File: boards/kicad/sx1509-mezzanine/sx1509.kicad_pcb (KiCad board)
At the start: 2 copper layers, 85 x 34.3 mm, 19 parts, among them J1 Conn_02x08_Odd_Even, J2 Conn_02x08_Odd_Even, J3 Conn_01x02_Male, J4 Conn_01x02_Male, P1 CONN_02X20, P2 CONN_02X20, U1 SX1509

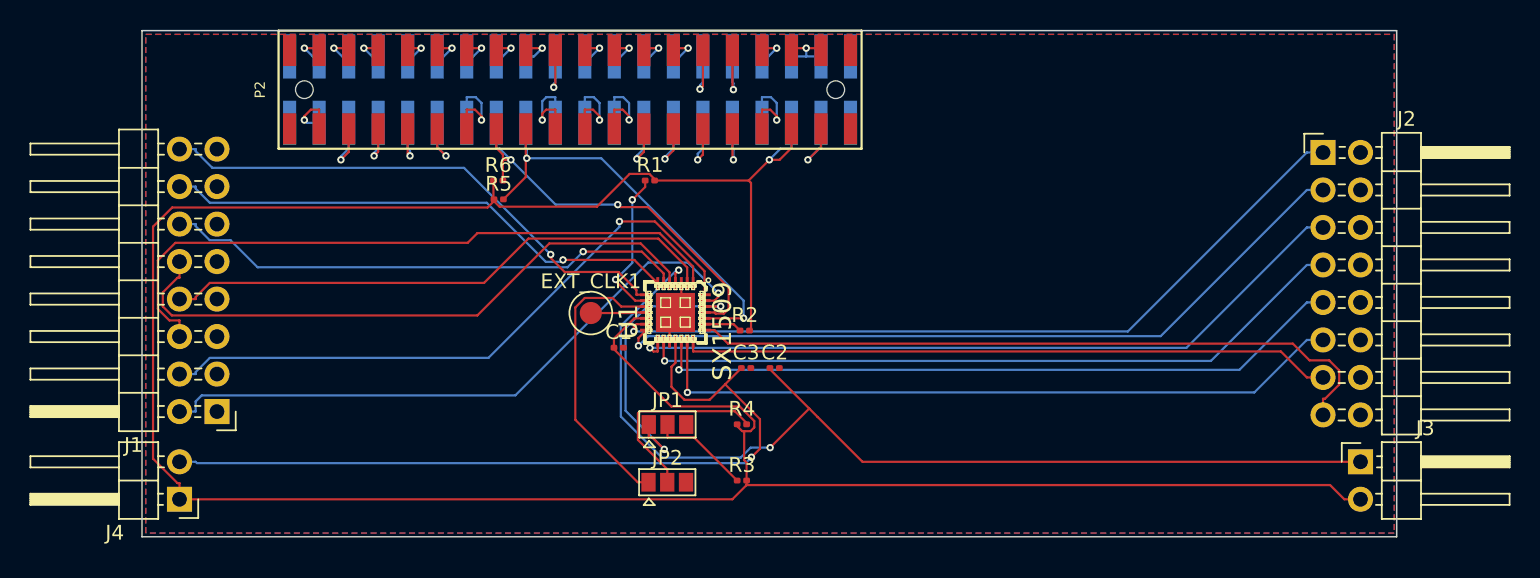
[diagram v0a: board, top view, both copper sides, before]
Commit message: Clean up design
The placement, routing, and silkscreen were updated to look nicer.
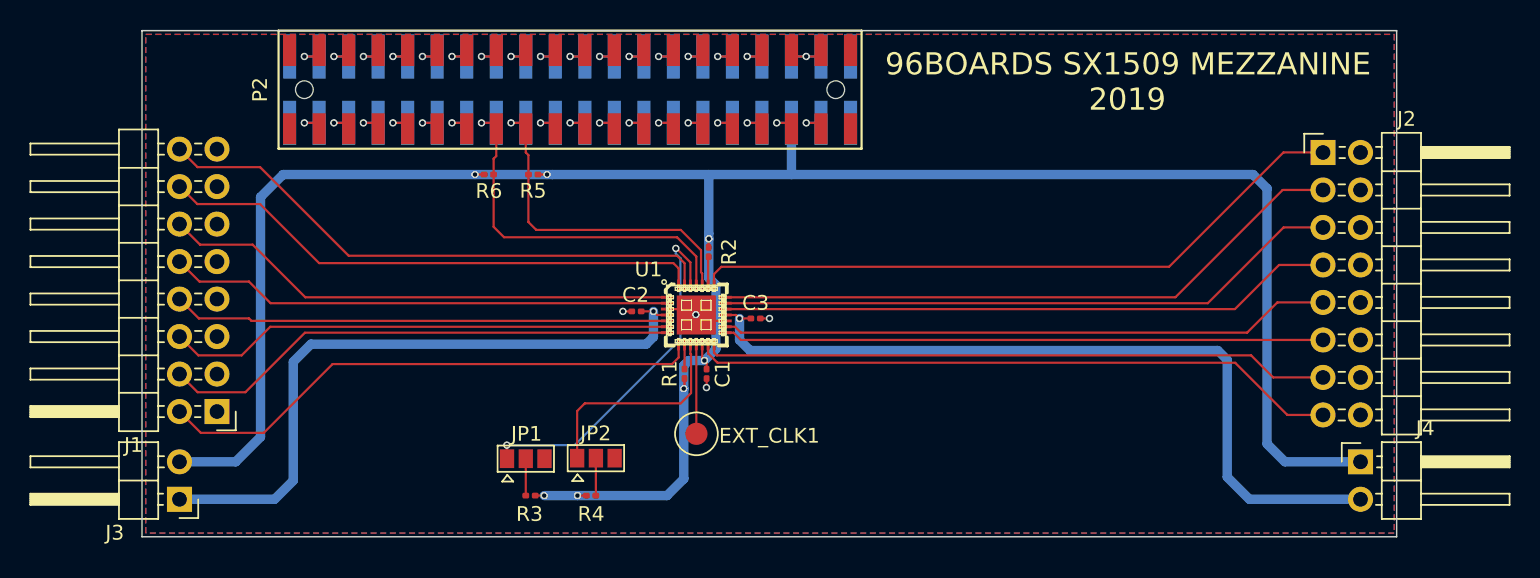
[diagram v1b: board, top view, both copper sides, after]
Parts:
- moved J3 80.1 mm to (102.5, 131.8), turned to 180 degrees
- moved J4 80.1 mm to (182.6, 129.2), turned to 0 degrees
- moved R3 14.4 mm to (126.3, 131.5)
- moved R1 13.3 mm to (136.8, 123.2), turned to 270 degrees
- moved R4 11.3 mm to (130.4, 131.5)
- moved EXT_CLK1 10.9 mm to (137.6, 127.3), turned to 90 degrees
- moved C2 10.1 mm to (133.5, 119.0), turned to 180 degrees
- moved JP1 9.87 mm to (126.0, 129.0)
- moved C1 6.21 mm to (138.2, 123.2), turned to 270 degrees
- moved R2 5.86 mm to (138.4, 115.0), turned to 90 degrees
- moved JP2 5.10 mm to (130.8, 129.0)
- moved C3 3.42 mm to (141.6, 119.5)
- moved R5 2.88 mm to (126.5, 109.8), turned to 180 degrees
- moved U1 1.43 mm to (137.6, 119.3), turned to 0 degrees
- moved R6 0.75 mm to (123.5, 109.8)
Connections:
- J1 pad 10: IO_4 -> IO_3
- J1 pad 12: IO_5 -> IO_2
- J1 pad 14: IO_6 -> IO_1
- J1 pad 16: IO_7 -> IO_0
- J1 pad 2: IO_0 -> IO_7
- J1 pad 4: IO_1 -> IO_6
- J1 pad 6: IO_2 -> IO_5
- J1 pad 8: IO_3 -> IO_4
- J2 pad 1: IO_8 -> IO_15
- J2 pad 11: IO_13 -> IO_10
- J2 pad 13: IO_14 -> IO_9
- J2 pad 15: IO_15 -> IO_8
- J2 pad 3: IO_9 -> IO_14
- J2 pad 5: IO_10 -> IO_13
- J2 pad 7: IO_11 -> IO_12
- J2 pad 9: IO_12 -> IO_11
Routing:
- net VCC1: track 70.6 -> 45.0 mm, vias 2 -> 1
- net +1V8: track 183.5 -> 159.3 mm, vias 1 -> 8
- net Net-(JP2-Pad2): track 13.3 -> 2.54 mm
- net IO_2: track 45.3 -> 35.1 mm
- net IO_10: track 50.3 -> 40.7 mm, vias 1 -> 0
- net IO_9: track 52.0 -> 42.5 mm, vias 1 -> 0
- net IO_8: track 52.9 -> 44.0 mm, vias 1 -> 0
- net Net-(R1-Pad1): track 10.3 -> 1.69 mm, vias 2 -> 0
- net IO_4: track 41.7 -> 33.7 mm
- net IO_11: track 48.6 -> 41.5 mm, vias 1 -> 0
- net I2C0_SDA: track 30.4 -> 23.5 mm, vias 2 -> 1
- net IO_1: track 43.1 -> 37.3 mm, vias 1 -> 0
- net IO_12: track 47.5 -> 41.7 mm, vias 1 -> 0
- net IO_13: track 48.0 -> 42.6 mm, vias 1 -> 0
- net ADDR0: track 19.7 -> 24.9 mm
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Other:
- board text added: "2019"
- board text added: "96BOARDS SX1509 MEZZANINE"

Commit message: Update SX1509 mezzanine silkscreen
Adds GPIO numbering to the silkscreen.
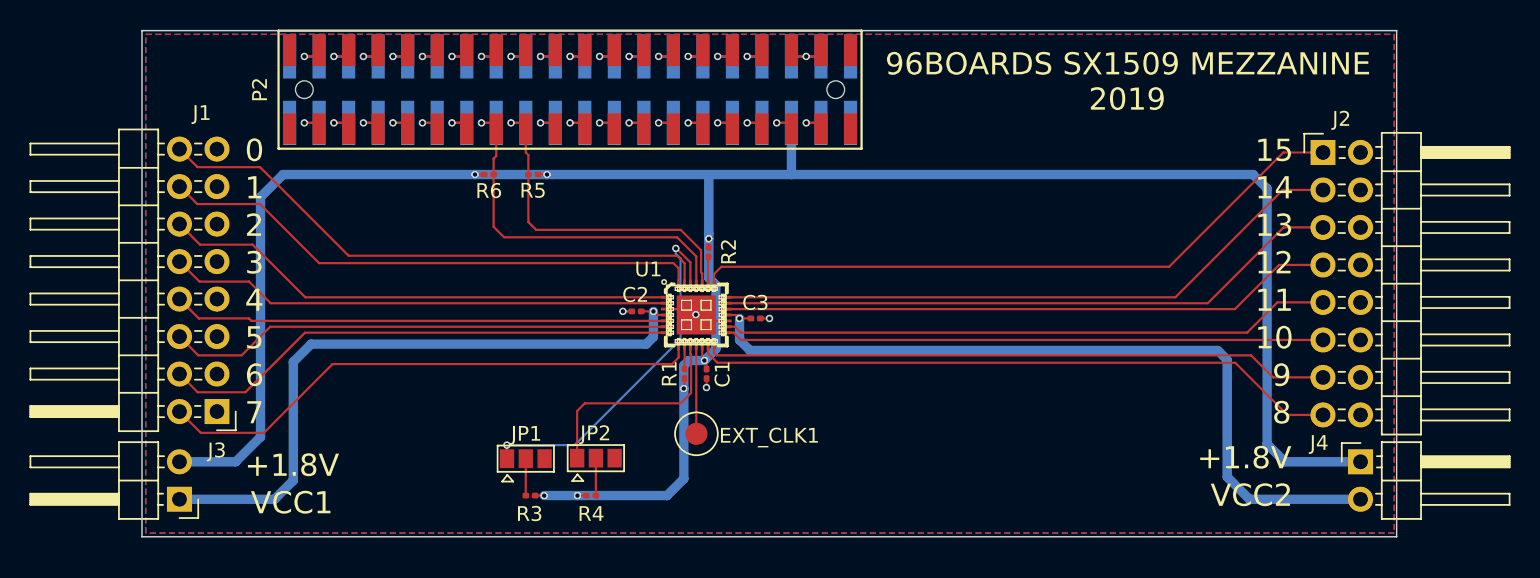
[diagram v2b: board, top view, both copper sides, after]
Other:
- board text added: "+1.8V"
- board text added: "0"
- board text added: "1"
- board text added: "10"
- board text added: "11"
- board text added: "12"
- board text added: "13"
- board text added: "14"
- board text added: "15"
- board text added: "2"
- board text added: "3"
- board text added: "4"
- board text added: "5"
- board text added: "6"
- board text added: "7"
- board text added: "8"
- board text added: "9"
- board text added: "VCC1"
- board text added: "VCC2"
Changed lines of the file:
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@@
   (general
     (thickness 1.6)
-    (drawings 12)
+    (drawings 32)
     (tracks 343)
     (zones 0)
@@
     (descr "Through hole angled pin header, 1x02, 2.54mm pitch, 6mm pin length, single row")
     (tags "Through hole angled pin header THT 1x02 2.54mm single row")
-    (fp_text reference J3 (at 4.385 -2.27 180) (layer F.SilkS)
+    (fp_text reference J3 (at -2.54 3.302 180) (layer F.SilkS)
       (effects (font (size 1 1) (thickness 0.15)))
     )
@@
     (descr "Through hole angled pin header, 1x02, 2.54mm pitch, 6mm pin length, single row")
     (tags "Through hole angled pin header THT 1x02 2.54mm single row")
-    (fp_text reference J4 (at 4.385 -2.27) (layer F.SilkS)
+    (fp_text reference J4 (at -2.794 -1.27) (layer F.SilkS)
       (effects (font (size 1 1) (thickness 0.15)))
     )
@@
     (descr "Through hole angled pin header, 2x08, 2.54mm pitch, 6mm pin length, double rows")
     (tags "Through hole angled pin header THT 2x08 2.54mm double row")
-    (fp_text reference J1 (at 5.655 -2.27 180) (layer F.SilkS)
+    (fp_text reference J1 (at 1.016 20.218 180) (layer F.SilkS)
       (effects (font (size 1 1) (thickness 0.15)))
     )
@@
     (descr "Through hole angled pin header, 2x08, 2.54mm pitch, 6mm pin length, double rows")
     (tags "Through hole angled pin header THT 2x08 2.54mm double row")
-    (fp_text reference J2 (at 5.655 -2.27) (layer F.SilkS)
+    (fp_text reference J2 (at 1.27 -2.27) (layer F.SilkS)
       (effects (font (size 1 1) (thickness 0.15)))
     )
@@
     )
   )
+  (gr_text VCC2 (at 175.184 131.496) (layer F.SilkS)
+    (effects (font (size 1.5 1.5) (thickness 0.3)))
+  )
+  (gr_text +1.8V (at 174.676 128.956) (layer F.SilkS)
+    (effects (font (size 1.5 1.5) (thickness 0.3)))
+  )
+  (gr_text VCC1 (at 110.16 132.004) (layer F.SilkS)
+    (effects (font (size 1.5 1.5) (thickness 0.3)))
+  )
+  (gr_text +1.8V (at 110.16 129.464) (layer F.SilkS)
+    (effects (font (size 1.5 1.5) (thickness 0.3)))
+  )
+  (gr_text 15 (at 176.708 108.128) (layer F.SilkS)
+    (effects (font (size 1.5 1.5) (thickness 0.3)))
+  )
+  (gr_text 14 (at 176.708 110.668) (layer F.SilkS)
+    (effects (font (size 1.5 1.5) (thickness 0.3)))
+  )
+  (gr_text 13 (at 176.708 113.208) (layer F.SilkS)
+    (effects (font (size 1.5 1.5) (thickness 0.3)))
+  )
+  (gr_text 12 (at 176.708 115.748) (layer F.SilkS)
+    (effects (font (size 1.5 1.5) (thickness 0.3)))
+  )
+  (gr_text 11 (at 176.708 118.288) (layer F.SilkS)
+    (effects (font (size 1.5 1.5) (thickness 0.3)))
+  )
+  (gr_text 10 (at 176.708 120.828) (layer F.SilkS)
+    (effects (font (size 1.5 1.5) (thickness 0.3)))
+  )
+  (gr_text 9 (at 177.216 123.368) (layer F.SilkS)
+    (effects (font (size 1.5 1.5) (thickness 0.3)))
+  )
+  (gr_text 8 (at 177.216 125.908) (layer F.SilkS)
+    (effects (font (size 1.5 1.5) (thickness 0.3)))
+  )
+  (gr_text 7 (at 107.62 125.908) (layer F.SilkS)
+    (effects (font (size 1.5 1.5) (thickness 0.3)))
+  )
+  (gr_text 6 (at 107.62 123.368) (layer F.SilkS)
+    (effects (font (size 1.5 1.5) (thickness 0.3)))
+  )
+  (gr_text 5 (at 107.62 120.828) (layer F.SilkS)
+    (effects (font (size 1.5 1.5) (thickness 0.3)))
+  )
+  (gr_text 4 (at 107.62 118.288) (layer F.SilkS)
+    (effects (font (size 1.5 1.5) (thickness 0.3)))
+  )
+  (gr_text 3 (at 107.62 115.748) (layer F.SilkS)
+    (effects (font (size 1.5 1.5) (thickness 0.3)))
+  )
+  (gr_text 2 (at 107.62 113.208) (layer F.SilkS)
+    (effects (font (size 1.5 1.5) (thickness 0.3)))
+  )
+  (gr_text 1 (at 107.62 110.668) (layer F.SilkS)
+    (effects (font (size 1.5 1.5) (thickness 0.3)))
+  )
+  (gr_text 0 (at 107.62 108.128) (layer F.SilkS)
+    (effects (font (size 1.5 1.5) (thickness 0.3)))
+  )
   (gr_text 2019 (at 166.75 104.66) (layer F.SilkS)
